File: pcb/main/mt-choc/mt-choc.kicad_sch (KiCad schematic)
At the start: 129 parts, among them SW1 SW_Push, SW10 SW_Push, SW11 SW_Push, SW12 SW_Push, SW13 SW_Push, SW14 SW_Push, SW15 SW_Push, SW16 SW_Push, SW17 SW_Push, SW18 SW_Push, SW19 SW_Push, SW2 SW_Push, SW20 SW_Push, SW21 SW_Push, SW22 SW_Push, SW23 SW_Push, SW24 SW_Push, SW25 SW_Push, SW26 SW_Push, SW27 SW_Push, SW28 SW_Push, SW29 SW_Push, SW3 SW_Push, SW30 SW_Push, SW31 SW_Push, SW32 SW_Push, SW33 SW_Push, SW34 SW_Push, SW35 SW_Push, SW36 SW_Push, SW37 SW_Push, SW38 SW_Push, SW39 SW_Push, SW4 SW_Push, SW40 SW_Push, SW41 SW_Push, SW42 SW_Push, SW43 SW_Push, SW44 SW_Push, SW45 SW_Push, SW46 SW_Push, SW47 SW_Push, SW48 SW_Push, SW49 SW_Push, SW5 SW_Push, SW50 SW_Push, SW51 SW_Push, SW52 SW_Push, SW53 SW_Push, SW54 SW_Push, SW55 SW_Push, SW56 SW_Push, SW57 SW_Push, SW58 SW_Push, SW59 SW_Push, SW6 SW_Push, SW60 SW_Push, SW61 SW_Push, SW62 SW_Push, SW63 SW_Push, SW64 SW_Push, SW7 SW_Push, SW8 SW_Push, SW9 SW_Push, U1 RP2040_LCD_1p28

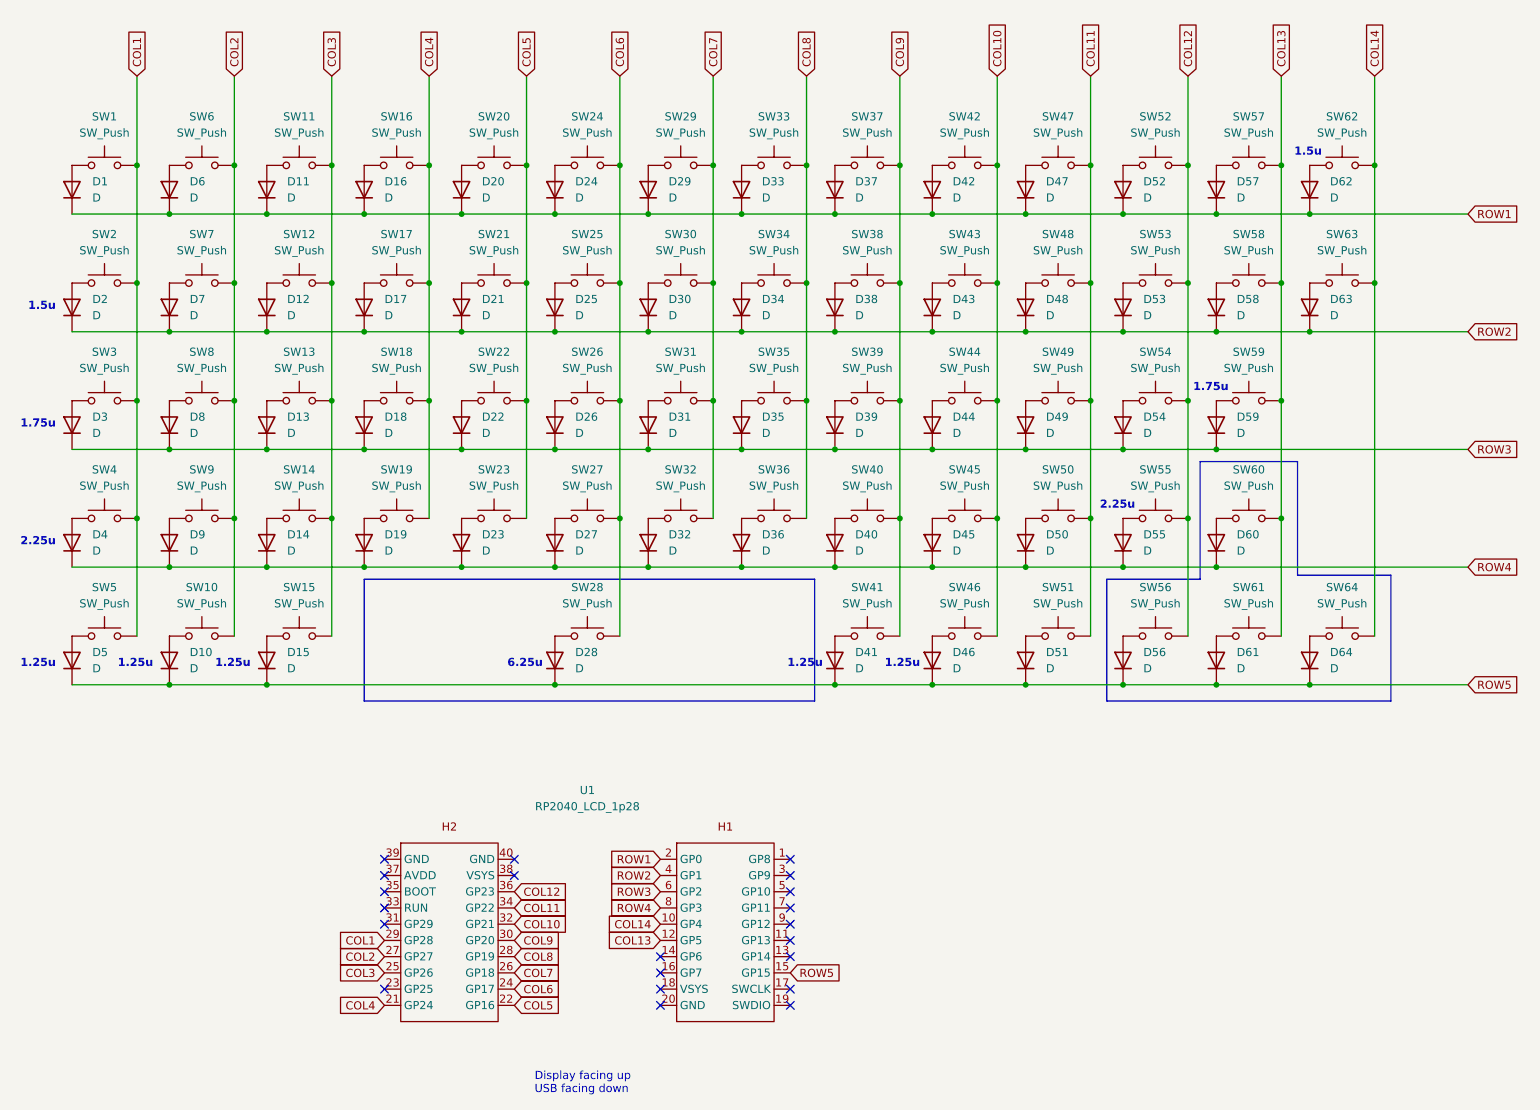
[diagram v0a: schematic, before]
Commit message: Split spacebar and more docs
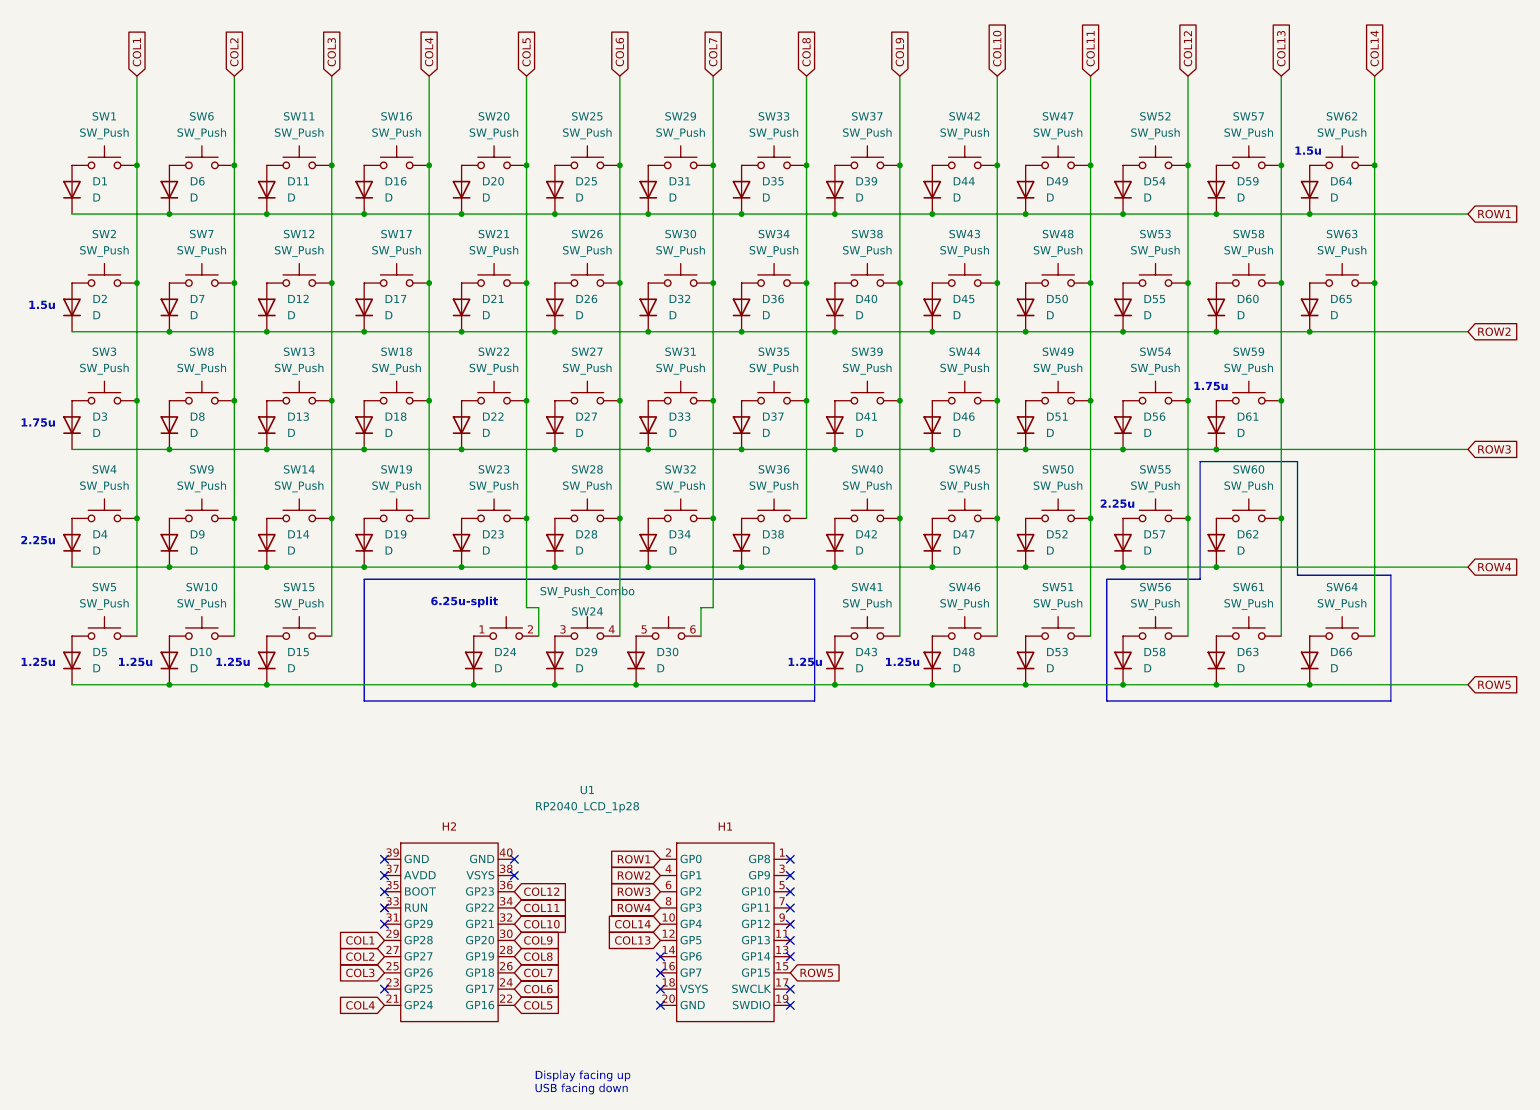
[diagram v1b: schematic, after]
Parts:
- removed SW28: SW_Push, symbol Switch:SW_Push
- added D29, D30: D, symbol Device:D
- added SW24: SW_Push_Combo, symbol mt-choc-symbols:choc-6.25u-split
- renumbered D28 to D24, D24 to D25, D25 to D26, D26 to D27, D27 to D28, D29 to D31, D30 to D32, D31 to D33, D32 to D34, D33 to D35, D34 to D36, D35 to D37, D36 to D38, D37 to D39, D38 to D40, D39 to D41, D40 to D42, D41 to D43, D42 to D44, D43 to D45, D44 to D46, D45 to D47, D46 to D48, D47 to D49, D48 to D50, D49 to D51, D50 to D52, D51 to D53, D52 to D54, D53 to D55, D54 to D56, D55 to D57, D56 to D58, D57 to D59, D58 to D60, D59 to D61, D60 to D62, D61 to D63, D62 to D64, D63 to D65, D64 to D66, SW24 to SW25, SW25 to SW26, SW26 to SW27, SW27 to SW28
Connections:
- net COL5: now also SW24.2
- net COL6: now also SW24.4
- net COL7: now also SW24.6
- net ROW5: now also D29.1 (K), D30.1 (K)
- net at D24.2 (A): now also SW24.1
- new net: D29.2 (A), SW24.3
- new net: D30.2 (A), SW24.5
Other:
- note added: "6.25u-split"
- note removed: "6.25u"
- moved on the sheet: D24

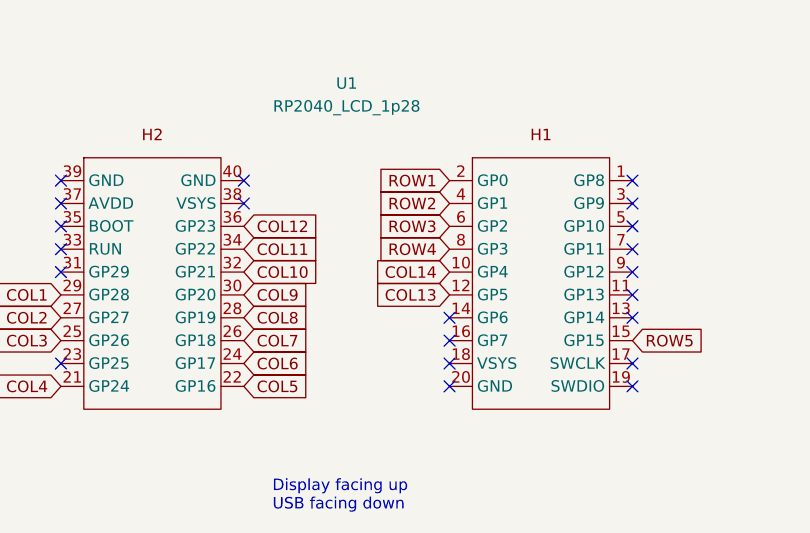
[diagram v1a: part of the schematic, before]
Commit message: Iniital layout for main PCB
- Update properties on footprints
- Main PCB is _technically_ done
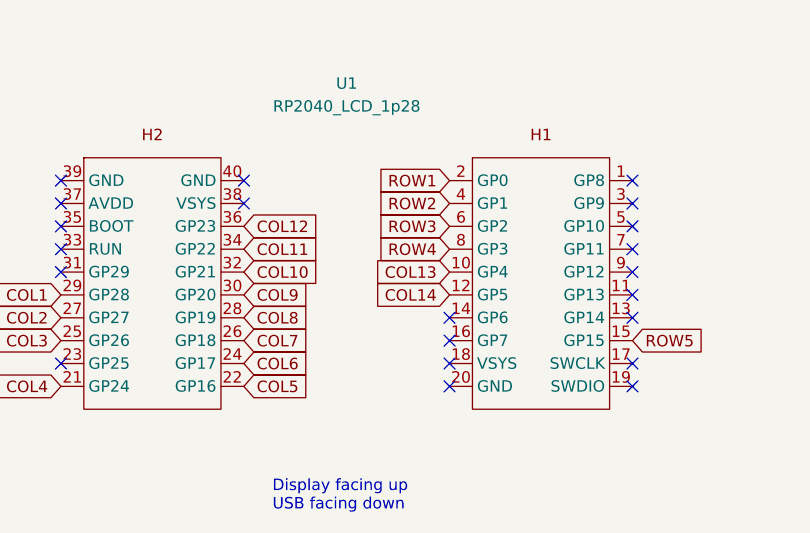
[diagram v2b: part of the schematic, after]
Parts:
- D1, D10, D11, D12, D13, D14, D15, D16, D17, D18, D19, D2, D20, D21, D22, D23, D24, D25, D26, D27, D28, D29, D3, D30, D31, D32, D33, D34, D35, D36, D37, D38, D39, D4, D40, D41, D42, D43, D44, D45, D46, D47, D48, D49, D5, D50, D51, D52, D53, D54, D55, D56, D57, D58, D59, D6, D60, D61, D62, D63, D64, D65, D66, D7, D8, D9: footprint (none) -> mt-choc-footprints:D_SOD123
- SW1, SW11, SW12, SW13, SW14, SW16, SW17, SW18, SW19, SW20, SW21, SW22, SW23, SW25, SW26, SW27, SW28, SW29, SW30, SW31, SW32, SW33, SW34, SW35, SW36, SW37, SW38, SW39, SW40, SW42, SW43, SW44, SW45, SW47, SW48, SW49, SW50, SW51, SW52, SW53, SW54, SW56, SW57, SW58, SW6, SW60, SW61, SW63, SW64, SW7, SW8, SW9: footprint (none) -> mt-choc-footprints:Choc-1u
- SW10, SW15, SW41, SW46, SW5: footprint (none) -> mt-choc-footprints:Choc-1.25u
- SW2, SW62: footprint (none) -> mt-choc-footprints:Choc-1.5u
- SW24: footprint (none) -> mt-choc-footprints:Choc-6.25u-split
- SW3, SW59: footprint (none) -> mt-choc-footprints:Choc-1.75u
- SW4, SW55: footprint (none) -> mt-choc-footprints:Choc-2.25u
- U1: footprint (none) -> mt-choc-footprints:RP2040_LCD_1p28
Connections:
- net COL13: now also U1.10 (GP4); no longer U1.12 (GP5)
- net COL14: now also U1.12 (GP5); no longer U1.10 (GP4)
